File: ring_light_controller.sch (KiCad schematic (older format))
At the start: 85 parts, among them J1 AudioJack2_Ground, J10 CHN_2_0, J11 CHN_2_1, J12 Color LED Port, J13 Conn_01x02, J2 CHAIN_IN, J3 CHAIN_OUT, J4 CHN_0_0, J5 CHN_0_1, J6 CHN_1_0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

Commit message: updated connecters to 3.5mm, and made opto resistors smaller in value
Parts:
- removed J2: CHAIN_IN, Connector_JST:JST_XH_B3B-XH-AM_1x03_P2.50mm_Vertical, symbol Connector_Generic:Conn_01x03
- removed J3: CHAIN_OUT, Connector_JST:JST_XH_B3B-XH-AM_1x03_P2.50mm_Vertical, symbol Connector_Generic:Conn_01x03
- added J2, J3: AudioJack3, justb:Jack_3.5mm_BOOMELE_C18594-SMT_Horizontal, symbol Connector:AudioJack3
- J9: footprint Connector_PinHeader_1.27mm:PinHeader_1x03_P1.27mm_Vertical -> Connector_PinHeader_2.54mm:PinHeader_1x03_P2.54mm_Vertical
- R10, R9: value 1k -> 200; LCSC C11702 -> C25087
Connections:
- net +24V: now also J10.2 (Pin_2), J11.2 (Pin_2), J4.2 (Pin_2), J5.2 (Pin_2), J6.2 (Pin_2), J7.2 (Pin_2); no longer J10.1 (Pin_1), J11.1 (Pin_1), J4.1 (Pin_1), J5.1 (Pin_1), J6.1 (Pin_1), J7.1 (Pin_1)
- net +5V: now also J12.3 (Pin_3); no longer J12.1 (Pin_1)
- net C_LED_CTRL: now also J12.1 (Pin_1); no longer J12.3 (Pin_3)
- net GND: now also J2.S, J3.S
- net LOAD_IN: now also J2.R
- net LOAD_OUT: now also J3.R
- net RX: now also J2.T
- net TX: now also J3.T
- net at Q4.3 (C): now also J4.1 (Pin_1); no longer J4.2 (Pin_2)
- net at Q8.3 (C): now also J6.1 (Pin_1); no longer J6.2 (Pin_2)
- net at Q12.3 (C): now also J10.1 (Pin_1); no longer J10.2 (Pin_2)
- net at Q5.3 (C): now also J5.1 (Pin_1); no longer J5.2 (Pin_2)
- net at Q9.3 (C): now also J7.1 (Pin_1); no longer J7.2 (Pin_2)
- net at Q13.3 (C): now also J11.1 (Pin_1); no longer J11.2 (Pin_2)
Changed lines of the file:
@@
 Title "Ring Light Controller v1"
 Date "2021-07-09"
-Rev "4"
+Rev "5"
 Comp "Brigham Young University HBLL"
 Comment1 ""
@@
 F 0 "J9" H 10980 1442 50  0000 L CNN
 F 1 "Program Port" H 10980 1351 50  0000 L CNN
-F 2 "Connector_PinHeader_1.27mm:PinHeader_1x03_P1.27mm_Vertical" H 10900 1400 50  0001 C CNN
+F 2 "Connector_PinHeader_2.54mm:PinHeader_1x03_P2.54mm_Vertical" H 10900 1400 50  0001 C CNN
 F 3 "~" H 10900 1400 50  0001 C CNN
 	1    10900 1400
@@
 L Connector_Generic:Conn_01x02 J4
 U 1 1 60FA39D7
-P 10950 5450
-F 0 "J4" H 11030 5442 50  0000 L CNN
-F 1 "CHN_0_0" H 11030 5351 50  0000 L CNN
-F 2 "Connector_JST:JST_XH_B2B-XH-AM_1x02_P2.50mm_Vertical" H 10950 5450 50  0001 C CNN
-F 3 "~" H 10950 5450 50  0001 C CNN
-	1    10950 5450
-	1    0    0    -1
+P 10950 5550
+F 0 "J4" H 11030 5542 50  0000 L CNN
+F 1 "CHN_0_0" H 11030 5451 50  0000 L CNN
+F 2 "Connector_JST:JST_XH_B2B-XH-AM_1x02_P2.50mm_Vertical" H 10950 5550 50  0001 C CNN
+F 3 "~" H 10950 5550 50  0001 C CNN
+	1    10950 5550
+	1    0    0    1
 $EndComp
 $Comp
@@
 L Connector_Generic:Conn_01x02 J6
 U 1 1 60FC0E5F
-P 13300 5450
-F 0 "J6" H 13380 5442 50  0000 L CNN
-F 1 "CHN_1_0" H 13380 5351 50  0000 L CNN
-F 2 "Connector_JST:JST_XH_B2B-XH-AM_1x02_P2.50mm_Vertical" H 13300 5450 50  0001 C CNN
-F 3 "~" H 13300 5450 50  0001 C CNN
-	1    13300 5450
-	1    0    0    -1
+P 13300 5550
+F 0 "J6" H 13380 5542 50  0000 L CNN
+F 1 "CHN_1_0" H 13380 5451 50  0000 L CNN
+F 2 "Connector_JST:JST_XH_B2B-XH-AM_1x02_P2.50mm_Vertical" H 13300 5550 50  0001 C CNN
+F 3 "~" H 13300 5550 50  0001 C CNN
+	1    13300 5550
+	1    0    0    1
 $EndComp
 $Comp
@@
 L Connector_Generic:Conn_01x02 J10
 U 1 1 60FC6AF5
-P 15600 5450
-F 0 "J10" H 15680 5442 50  0000 L CNN
-F 1 "CHN_2_0" H 15680 5351 50  0000 L CNN
-F 2 "Connector_JST:JST_XH_B2B-XH-AM_1x02_P2.50mm_Vertical" H 15600 5450 50  0001 C CNN
-F 3 "~" H 15600 5450 50  0001 C CNN
-	1    15600 5450
-	1    0    0    -1
+P 15600 5550
+F 0 "J10" H 15680 5542 50  0000 L CNN
+F 1 "CHN_2_0" H 15680 5451 50  0000 L CNN
+F 2 "Connector_JST:JST_XH_B2B-XH-AM_1x02_P2.50mm_Vertical" H 15600 5550 50  0001 C CNN
+F 3 "~" H 15600 5550 50  0001 C CNN
+	1    15600 5550
+	1    0    0    1
 $EndComp
 $Comp
@@
 $EndComp
 $Comp
-L Connector_Generic:Conn_01x02 J5
-U 1 1 60FE049F
-P 10950 7500
-F 0 "J5" H 11030 7492 50  0000 L CNN
-F 1 "CHN_0_1" H 11030 7401 50  0000 L CNN
-F 2 "Connector_JST:JST_XH_B2B-XH-AM_1x02_P2.50mm_Vertical" H 10950 7500 50  0001 C CNN
-F 3 "~" H 10950 7500 50  0001 C CNN
-	1    10950 7500
-	1    0    0    -1
-$EndComp
-$Comp
 L Transistor_BJT:MMBT5551L Q9
 U 1 1 60FE04A5
@@
 $EndComp
 $Comp
-L Connector_Generic:Conn_01x02 J7
-U 1 1 60FE04E6
-P 13300 7500
-F 0 "J7" H 13380 7492 50  0000 L CNN
-F 1 "CHN_1_1" H 13380 7401 50  0000 L CNN
-F 2 "Connector_JST:JST_XH_B2B-XH-AM_1x02_P2.50mm_Vertical" H 13300 7500 50  0001 C CNN
-F 3 "~" H 13300 7500 50  0001 C CNN
-	1    13300 7500
-	1    0    0    -1
-$EndComp
-$Comp
 L Transistor_BJT:MMBT5551L Q13
 U 1 1 60FE04EC
@@
 L Connector_Generic:Conn_01x02 J11
 U 1 1 60FE052D
-P 15600 7500
-F 0 "J11" H 15680 7492 50  0000 L CNN
-F 1 "CHN_2_1" H 15680 7401 50  0000 L CNN
-F 2 "Connector_JST:JST_XH_B2B-XH-AM_1x02_P2.50mm_Vertical" H 15600 7500 50  0001 C CNN
-F 3 "~" H 15600 7500 50  0001 C CNN
-	1    15600 7500
-	1    0    0    -1
+P 15600 7600
+F 0 "J11" H 15680 7592 50  0000 L CNN
+F 1 "CHN_2_1" H 15680 7501 50  0000 L CNN
+F 2 "Connector_JST:JST_XH_B2B-XH-AM_1x02_P2.50mm_Vertical" H 15600 7600 50  0001 C CNN
+F 3 "~" H 15600 7600 50  0001 C CNN
+	1    15600 7600
+	1    0    0    1
 $EndComp
 Text GLabel 9300 5250 0    50   Input ~ 0
@@
 	0    -1   -1   0
 $EndComp
-$Comp
-L Connector_Generic:Conn_01x03 J2
-U 1 1 612E0055
-P 7100 3600
-F 0 "J2" H 7180 3642 50  0000 L CNN
-F 1 "CHAIN_IN" H 7180 3551 50  0000 L CNN
-F 2 "Connector_JST:JST_XH_B3B-XH-AM_1x03_P2.50mm_Vertical" H 7100 3600 50  0001 C CNN
-F 3 "~" H 7100 3600 50  0001 C CNN
-	1    7100 3600
-	1    0    0    -1
-$EndComp
-$Comp
-L Connector_Generic:Conn_01x03 J3
-U 1 1 612E1139
-P 11100 3600
-F 0 "J3" H 11180 3642 50  0000 L CNN
-F 1 "CHAIN_OUT" H 11180 3551 50  0000 L CNN
-F 2 "Connector_JST:JST_XH_B3B-XH-AM_1x03_P2.50mm_Vertical" H 11100 3600 50  0001 C CNN
-F 3 "~" H 11100 3600 50  0001 C CNN
-	1    11100 3600
-	1    0    0    -1
-$EndComp
 Text GLabel 8550 3100 0    50   Input ~ 0
 LOAD_IN
@@
 	1    0    0    -1
 $EndComp
-Wire Wire Line
-	6900 3600 6750 3600
-Wire Wire Line
-	10900 3600 10750 3600
 $Comp
 L power:GND #PWR018
 U 1 1 61391CE0
-P 6750 3600
-F 0 "#PWR018" H 6750 3350 50  0001 C CNN
-F 1 "GND" V 6755 3472 50  0000 R CNN
-F 2 "" H 6750 3600 50  0001 C CNN
-F 3 "" H 6750 3600 50  0001 C CNN
-	1    6750 3600
+P 6850 3700
+F 0 "#PWR018" H 6850 3450 50  0001 C CNN
+F 1 "GND" V 6855 3572 50  0000 R CNN
+F 2 "" H 6850 3700 50  0001 C CNN
+F 3 "" H 6850 3700 50  0001 C CNN
+	1    6850 3700
 	0    1    -1   0
 $EndComp
-Text GLabel 6900 3700 0    50   Input ~ 0
+Text GLabel 6850 3600 0    50   Input ~ 0
 LOAD_IN
-Text GLabel 10900 3700 0    50   Input ~ 0
+Text GLabel 10550 3600 0    50   Input ~ 0
 LOAD_OUT
 $Comp
 L power:GND #PWR019
 U 1 1 613BBAF4
-P 10750 3600
-F 0 "#PWR019" H 10750 3350 50  0001 C CNN
-F 1 "GND" V 10755 3472 50  0000 R CNN
-F 2 "" H 10750 3600 50  0001 C CNN
-F 3 "" H 10750 3600 50  0001 C CNN
-	1    10750 3600
+P 10550 3700
+F 0 "#PWR019" H 10550 3450 50  0001 C CNN
+F 1 "GND" V 10555 3572 50  0000 R CNN
+F 2 "" H 10550 3700 50  0001 C CNN
+F 3 "" H 10550 3700 50  0001 C CNN
+	1    10550 3700
 	0    1    -1   0
 $EndComp
@@
 Wire Wire Line
 	9000 3350 9000 3450
-Text GLabel 6900 3500 0    50   Input ~ 0
+Text GLabel 6850 3500 0    50   Input ~ 0
 RX
-Text GLabel 10900 3500 0    50   Input ~ 0
+Text GLabel 10550 3500 0    50   Input ~ 0
 TX
 Text GLabel 3250 8600 2    50   Input ~ 0
@@
 P 2450 2050
 F 0 "R9" V 2245 2050 50  0000 C CNN
-F 1 "1k" V 2336 2050 50  0000 C CNN
+F 1 "200" V 2336 2050 50  0000 C CNN
 F 2 "Resistor_SMD:R_0402_1005Metric" V 2490 2040 50  0001 C CNN
 F 3 "~" H 2450 2050 50  0001 C CNN
 F 4 "C11702" H 2450 2050 50  0001 C CNN "LCSC Part #"
-F 5 "C11702" H 2450 2050 50  0001 C CNN "LCSC"
+F 5 "C25087" H 2450 2050 50  0001 C CNN "LCSC"
 	1    2450 2050
 	0    1    1    0
@@
 P 2450 2600
 F 0 "R10" V 2245 2600 50  0000 C CNN
-F 1 "1k" V 2336 2600 50  0000 C CNN
+F 1 "200" V 2336 2600 50  0000 C CNN
 F 2 "Resistor_SMD:R_0402_1005Metric" V 2490 2590 50  0001 C CNN
 F 3 "~" H 2450 2600 50  0001 C CNN
 F 4 "C11702" H 2450 2600 50  0001 C CNN "LCSC Part #"
-F 5 "C11702" H 2450 2600 50  0001 C CNN "LCSC"
+F 5 "C25087" H 2450 2600 50  0001 C CNN "LCSC"
 	1    2450 2600
 	0    1    1    0
@@
 F 3 "~" H 10900 2200 50  0001 C CNN
 	1    10900 2200
-	1    0    0    -1
+	1    0    0    1
 $EndComp
 Wire Wire Line
@@
 F 1 "AudioJack2_Ground" H 3670 2517 50  0000 R CNN
 F 2 "justb:Jack_2.5mm_PJ-2342-SMT" H 3850 2500 50  0001 C CNN
-F 3 "~" H 3850 2500 50  0001 C CNN
+F 3 "https://datasheet.lcsc.com/lcsc/1912111437_XKB-Connectivity-PJ-2342-SMT_C397356.pdf" H 3850 2500 50  0001 C CNN
 F 4 "C397356" H 3850 2500 50  0001 C CNN "LCSC Part #"
 F 5 "C397356" H 3850 2500 50  0001 C CNN "LCSC"
@@
 $EndComp
 Connection ~ 13250 3400
+$Comp
+L Connector_Generic:Conn_01x02 J7
+U 1 1 60FE04E6
+P 13300 7600
+F 0 "J7" H 13380 7592 50  0000 L CNN
+F 1 "CHN_1_1" H 13380 7501 50  0000 L CNN
+F 2 "Connector_JST:JST_XH_B2B-XH-AM_1x02_P2.50mm_Vertical" H 13300 7600 50  0001 C CNN
+F 3 "~" H 13300 7600 50  0001 C CNN
+	1    13300 7600
+	1    0    0    1
+$EndComp
+$Comp
+L Connector_Generic:Conn_01x02 J5
+U 1 1 60FE049F
+P 10950 7600
+F 0 "J5" H 11030 7592 50  0000 L CNN
+F 1 "CHN_0_1" H 11030 7501 50  0000 L CNN
+F 2 "Connector_JST:JST_XH_B2B-XH-AM_1x02_P2.50mm_Vertical" H 10950 7600 50  0001 C CNN
+F 3 "~" H 10950 7600 50  0001 C CNN
+	1    10950 7600
+	1    0    0    1
+$EndComp
+$Comp
+L Graphic:Logo_Open_Hardware_Small #LOGO1
+U 1 1 611AA3E5
+P 900 10200
+F 0 "#LOGO1" H 900 10475 50  0001 C CNN
+F 1 "Logo_Open_Hardware_Small" H 900 9975 50  0001 C CNN
+F 2 "" H 900 10200 50  0001 C CNN
+F 3 "~" H 900 10200 50  0001 C CNN
+	1    900  10200
+	1    0    0    -1
+$EndComp
+$Comp
+L Graphic:SYM_ESD_Large #SYM1
+U 1 1 611AB487
+P 1450 10150
+F 0 "#SYM1" H 1450 10350 50  0001 C CNN
+F 1 "SYM_ESD_Large" H 1450 9900 50  0001 C CNN
+F 2 "" H 1445 10120 50  0001 C CNN
+F 3 "~" H 1445 10120 50  0001 C CNN
+	1    1450 10150
+	1    0    0    -1
+$EndComp
+Wire Wire Line
+	6850 3500 6900 3500
+Wire Wire Line
+	6850 3600 6900 3600
+Wire Wire Line
+	10550 3600 10600 3600
+Wire Wire Line
+	10550 3500 10600 3500
+$Comp
+L Connector:AudioJack3 J2
+U 1 1 61284FE6
+P 7100 3600
+F 0 "J2" H 6820 3533 50  0000 R CNN
+F 1 "AudioJack3" H 6820 3624 50  0000 R CNN
+F 2 "justb:Jack_3.5mm_BOOMELE_C18594-SMT_Horizontal" H 7100 3600 50  0001 C CNN
+F 3 "~" H 7100 3600 50  0001 C CNN
+	1    7100 3600
+	-1   0    0    1
+$EndComp
+Wire Wire Line
+	6850 3700 6900 3700
+$Comp
+L Connector:AudioJack3 J3
+U 1 1 612A2C7A
+P 10800 3600
+F 0 "J3" H 10520 3533 50  0000 R CNN
+F 1 "AudioJack3" H 10520 3624 50  0000 R CNN
+F 2 "justb:Jack_3.5mm_BOOMELE_C18594-SMT_Horizontal" H 10800 3600 50  0001 C CNN
+F 3 "~" H 10800 3600 50  0001 C CNN
+	1    10800 3600
+	-1   0    0    1
+$EndComp
+Wire Wire Line
+	10600 3700 10550 3700
 $EndSCHEMATC

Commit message: slight changes
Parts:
- added D10, D11, D9: Green, LED_SMD:LED_0603_1608Metric, symbol Device:LED
- added R34, R8: 1k, Resistor_SMD:R_0402_1005Metric, symbol Device:R_US
- added R6: 1k, Resistor_SMD:R_0603_1608Metric, symbol Device:R_US
- added TP2, TP3, TP6: TestPoint, TestPoint:TestPoint_Pad_D1.0mm, symbol Connector:TestPoint
- J2, J3: LCSC (none) -> C18594; LCSC Part # (none) -> C18594
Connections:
- net +24V: now also TP6.1
- net +5V: now also R34.2, R8.2
- net GND: now also D9.1 (K)
- net LOAD_IN: now also R6.2
- net RX: now also D10.1 (K), TP2.1
- net TX: now also D11.1 (K), TP3.1
- new net: D9.2 (A), R6.1
- new net: D11.2 (A), R34.1
- new net: D10.2 (A), R8.1
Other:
- moved on the sheet: D1, D2, D3, D4, D5, D7, D8, Q1, R1, R11, R2, R3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

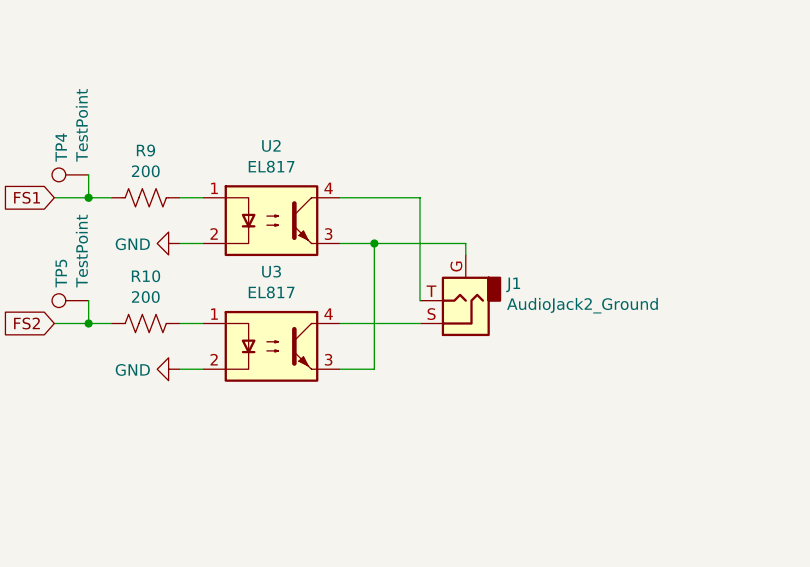
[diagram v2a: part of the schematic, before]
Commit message: fixed opto pin outputs
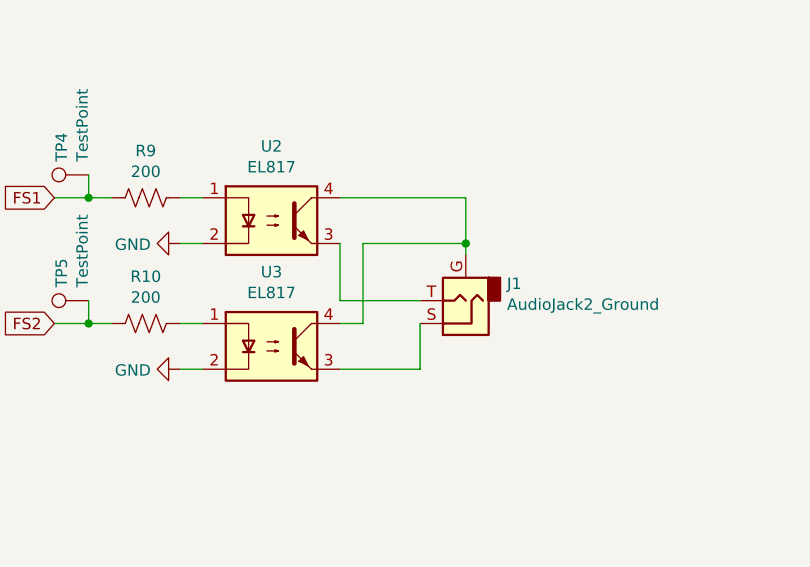
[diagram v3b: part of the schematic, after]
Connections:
- net at U3.4: now also J1.G, U2.4; no longer J1.S
- net at J1.T: now also U2.3; no longer U2.4
- new net: J1.S, U3.3
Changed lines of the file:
@@
 $EndComp
-Wire Wire Line
-	3300 2600 3650 2600
-Wire Wire Line
-	3300 2050 3650 2050
-Wire Wire Line
-	3650 2050 3650 2500
 Wire Wire Line
 	2700 2250 2600 2250
@@
 Wire Wire Line
 	6950 1950 6950 2000
-Wire Wire Line
-	3850 2250 3850 2300
-Wire Wire Line
-	3450 2800 3300 2800
-Wire Wire Line
-	3450 2250 3850 2250
-Wire Wire Line
-	3450 2250 3450 2800
-Connection ~ 3450 2250
-Wire Wire Line
-	3300 2250 3450 2250
 $Comp
 L Connector:AudioJack2_Ground J1
@@
 Wire Wire Line
 	6600 5550 6400 5550
+Wire Wire Line
+	3850 2050 3850 2250
+Wire Wire Line
+	3300 2050 3850 2050
+Wire Wire Line
+	3300 2600 3400 2600
+Wire Wire Line
+	3400 2600 3400 2250
+Wire Wire Line
+	3400 2250 3850 2250
+Connection ~ 3850 2250
+Wire Wire Line
+	3850 2250 3850 2300
+Wire Wire Line
+	3300 2250 3300 2500
+Wire Wire Line
+	3300 2500 3650 2500
+Wire Wire Line
+	3300 2800 3650 2800
+Wire Wire Line
+	3650 2800 3650 2600
 $EndSCHEMATC

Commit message: updated to latest
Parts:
- added R35, R36, R37, R38, R39, R40: 1k, Resistor_SMD:R_0402_1005Metric, symbol Device:R_US
- R11, R13, R14, R15, R16, R19, R20, R21, R22, R25, R26, R28, R29, R7: LCSC C11702 -> C21190; LCSC Part # C11702 -> C21190
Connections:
- net CHN_0_CTRL: now also R35.2, R36.2
- net CHN_1_CTRL: now also R37.2, R38.2
- net CHN_2_CTRL: now also R39.2, R40.2
- net GND: now also R35.1, R36.1, R37.1, R38.1, R39.1, R40.1
